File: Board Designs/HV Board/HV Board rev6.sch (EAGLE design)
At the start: 63 parts, among them IC1 OKI-78SR, IC2 NE5532SOIC

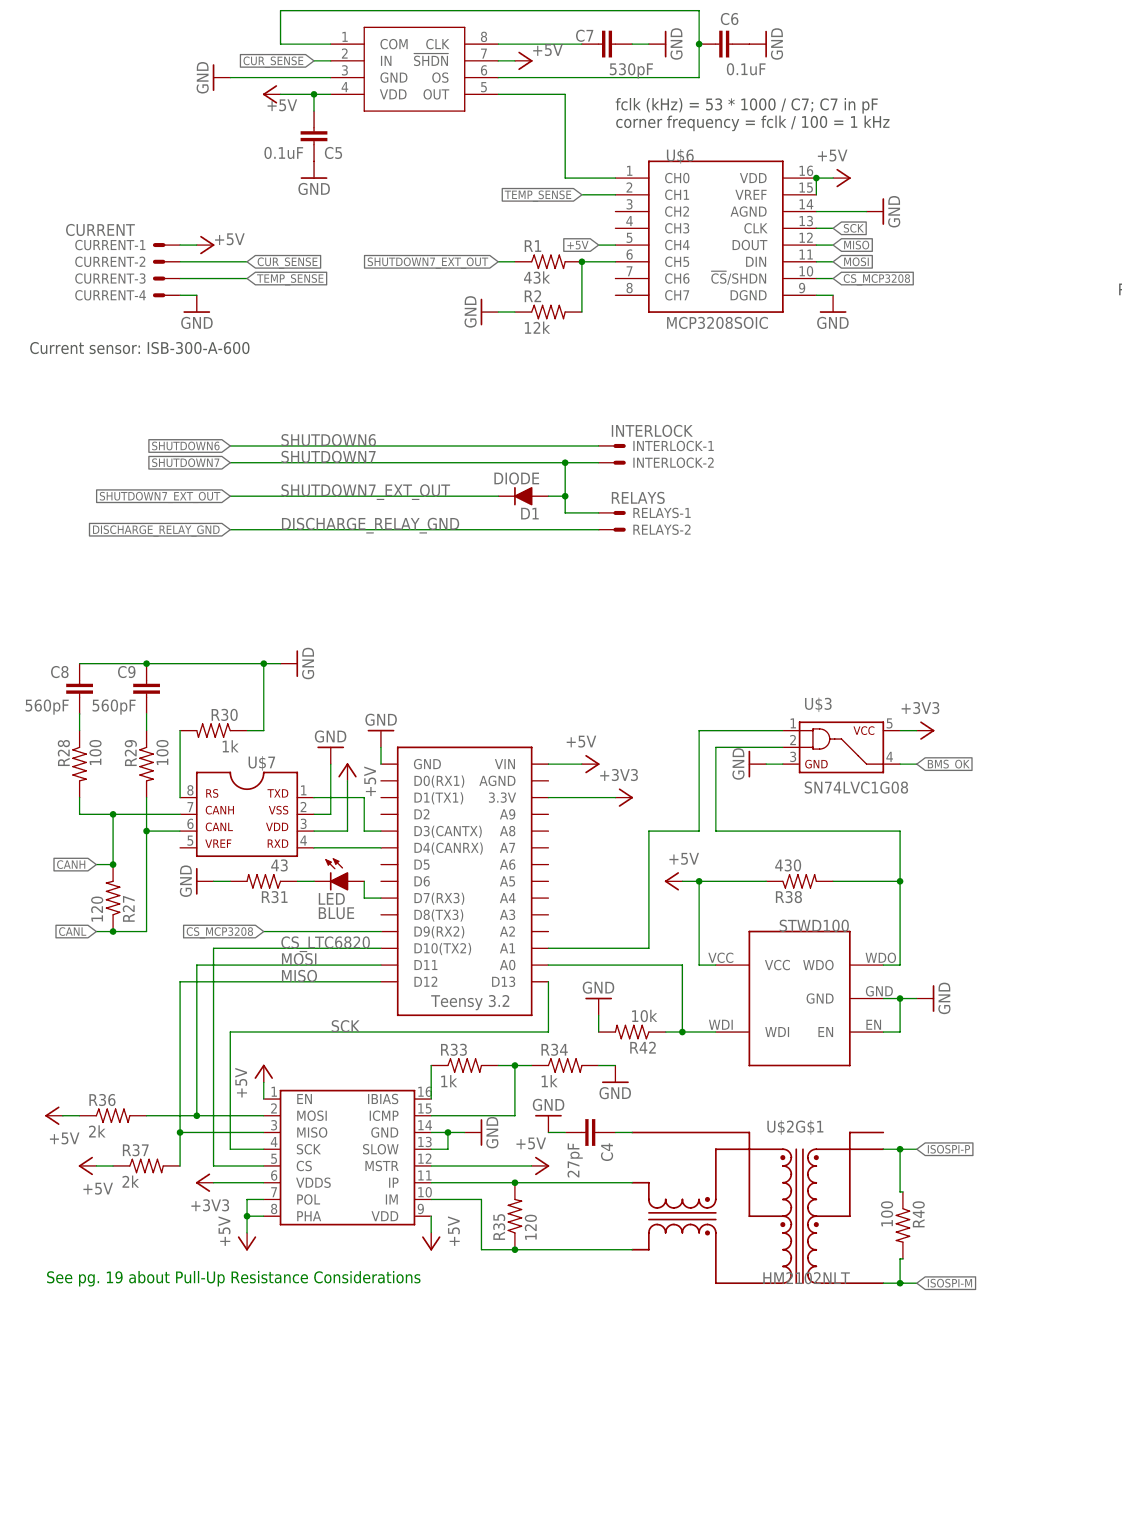
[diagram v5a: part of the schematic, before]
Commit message: HV rev 6&7: added TXB0104 to fix MSP 3208 voltage issue
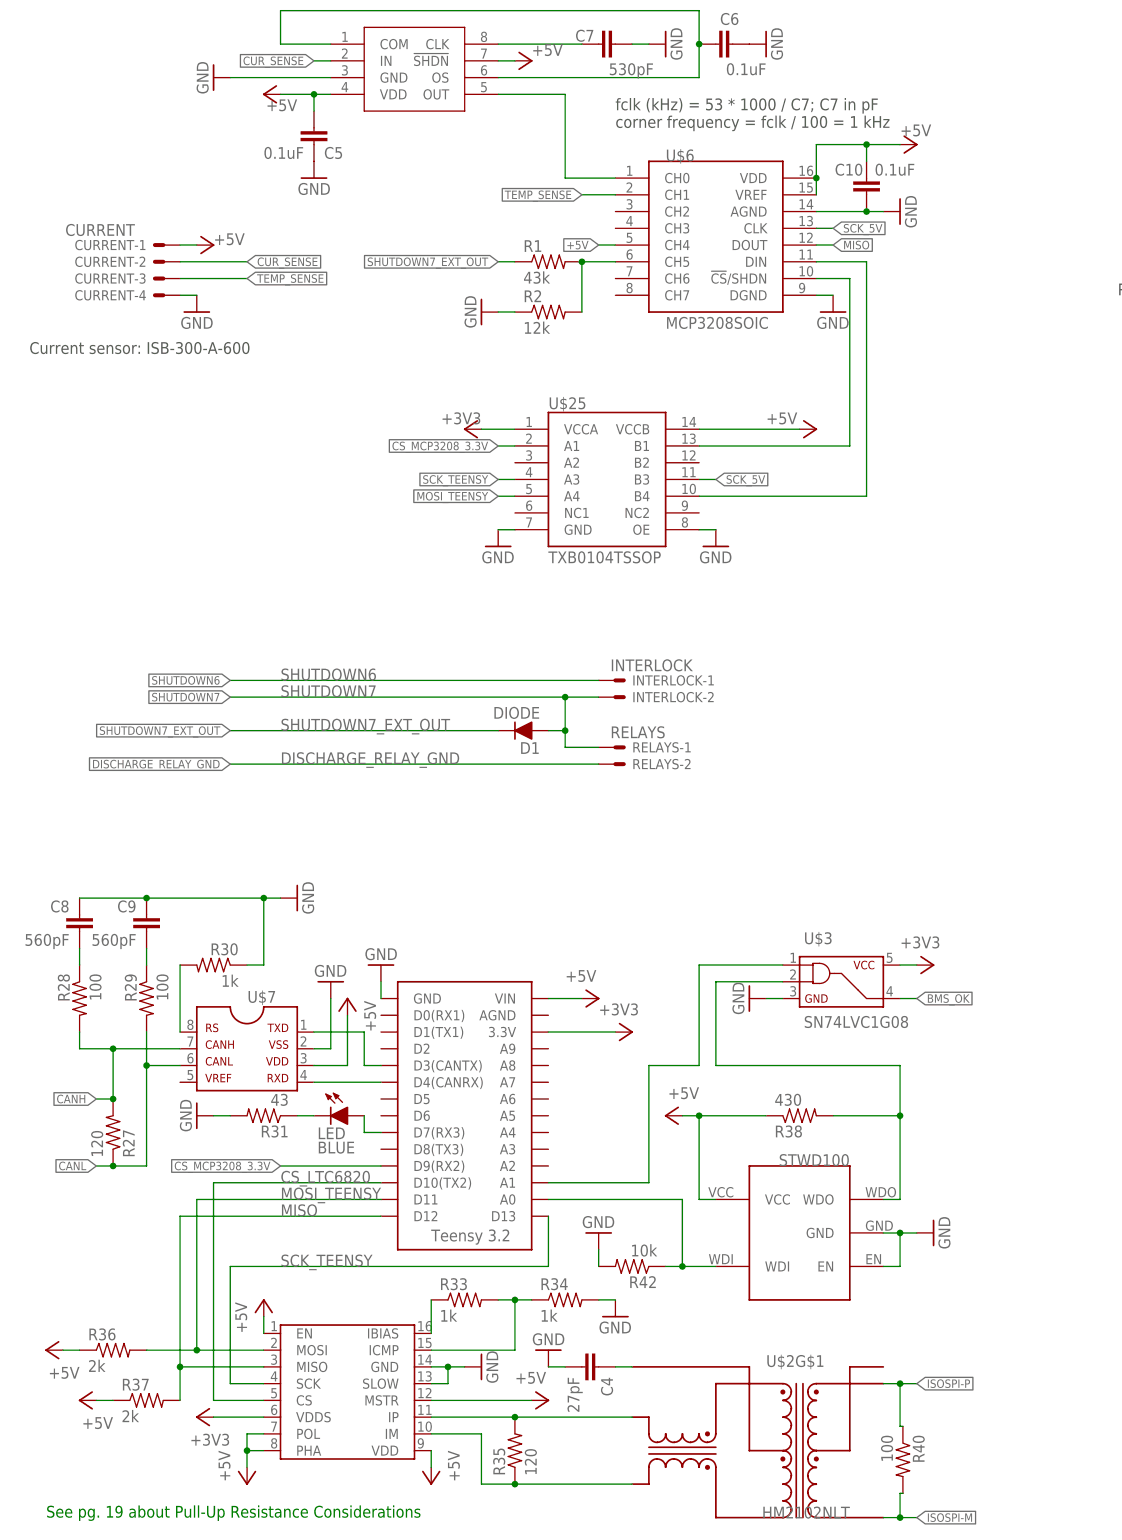
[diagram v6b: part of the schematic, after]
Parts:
- added C10: 0.1uF, HyTechDevices:CAP0805
- added U$25: TXB0104TSSOP, HyTechDevices:TXB0104TSSOP
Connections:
- removed net CS_MCP3208: U$6.!CS!/SHDN, U$9.D9(RX2)
- removed net MOSI: R36.2, U$6.DIN, U$8.MOSI, U$9.D11
- removed net SCK: U$6.CLK, U$8.SCK, U$9.D13
- new net CS_MCP3208_3.3V: U$25.A1, U$9.D9(RX2)
- new net MOSI_5V: U$25.B4, U$6.DIN
- new net MOSI_TEENSY: R36.2, U$25.A4, U$8.MOSI, U$9.D11
- new net N$7: U$25.B1, U$6.!CS!/SHDN
- new net SCK_5V: U$25.B3, U$6.CLK
- new net SCK_TEENSY: U$25.A3, U$8.SCK, U$9.D13
- net +3V3: now also U$25.VCCA
- net +5V: now also C10.2, U$25.VCCB
- net GND: now also C10.1, U$25.GND, U$25.OE
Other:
- moved on the sheet: C4, C8, C9, D1, INTERLOCK-1, INTERLOCK-2, LED, R27, R28, R29, R30, R31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
